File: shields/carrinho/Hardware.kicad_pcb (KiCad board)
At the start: 2 copper layers, 135.8 x 56.1 mm, 87 parts, among them J1 Conn_01x02, J10 Conn_01x04, J11 Conn_01x04, J12 Conn_02x13_Odd_Even, J13 Conn_01x02, J14 Conn_01x02, J2 Conn_01x04, J3 Conn_01x02, J4 Conn_01x02_Male, J5 Conn_01x02_Male, J6 Conn_01x02_Male, J7 Conn_01x02_Male, J8 Conn_01x03, J9 Conn_01x03, Q1 BD140, Q10 BC548, Q11 BD139, Q12 BD139, Q2 BD140, Q3 BC548, Q4 BC548, Q5 BD139, Q6 BD139, Q7 BD140, Q8 BD140, Q9 BC548, U1 LM393, U2 TCRT5000, U3 LM324, U4 HC-05, U5 TCRT5000

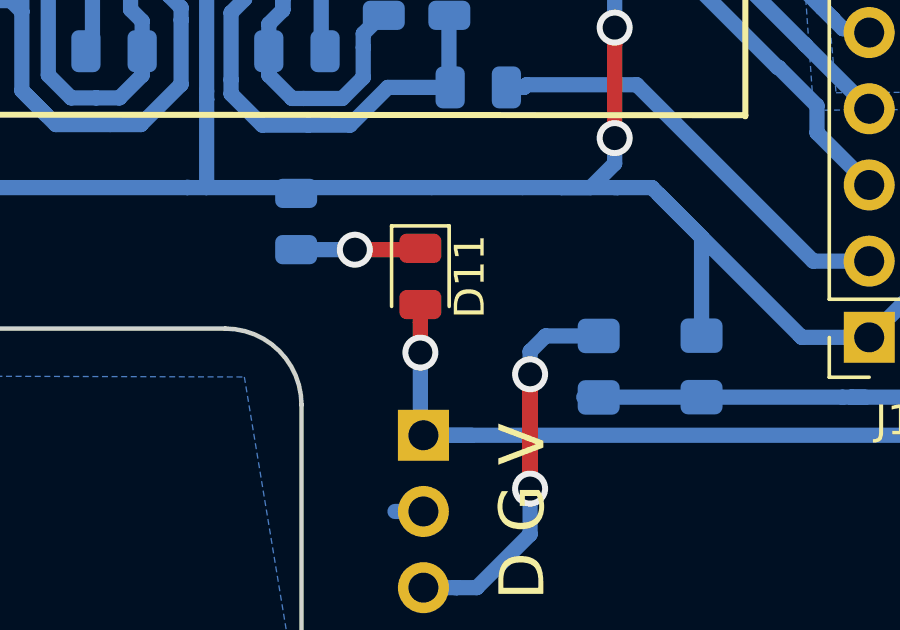
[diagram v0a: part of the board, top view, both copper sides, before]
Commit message: Adicionado exmplos com IRQ da USART.
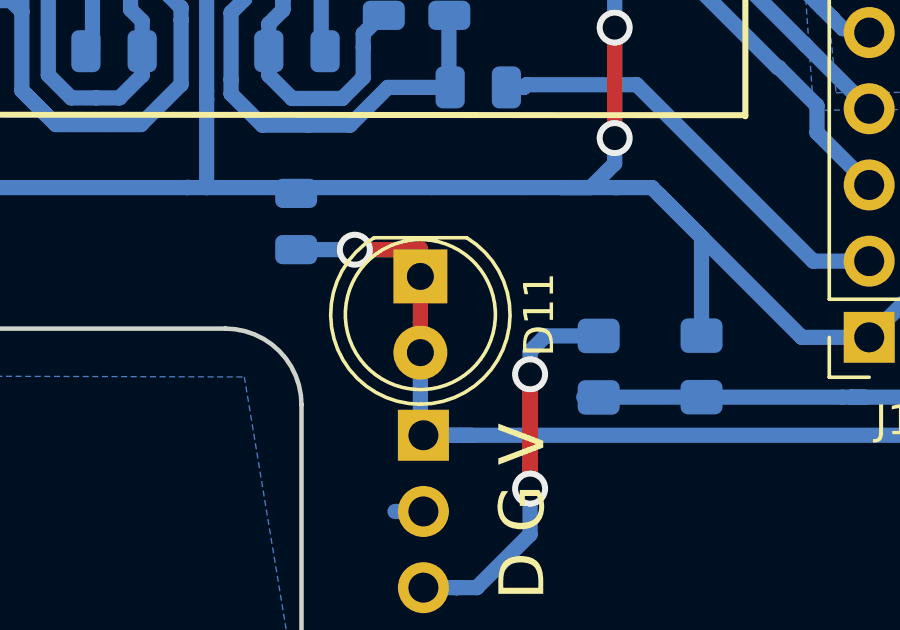
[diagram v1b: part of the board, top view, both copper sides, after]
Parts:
- D11: footprint LED_SMD:LED_0805_2012Metric -> LED_THT:LED_D5.0mm
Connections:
- D12 pad 1: +BATT -> Net-(D12-Pad1)
- D12 pad 2: Net-(D12-Pad2) -> +BATT
- J2 pad 1: Net-(D12-Pad2) -> +BATT
- J6 pad 1: +BATT -> Net-(D12-Pad1)
- J6 pad 2: +BATT -> Net-(D12-Pad1)
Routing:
- net Net-(D12-Pad2): track 4.70 -> 0.00 mm
- net +BATT: track 176.8 -> 181.5 mm
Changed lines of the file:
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@@
   (net 66 "Net-(D10-Pad2)")
   (net 67 "Net-(D11-Pad1)")
-  (net 68 "Net-(D12-Pad2)")
+  (net 68 "Net-(D12-Pad1)")
   (net_class Default "Esta é a classe de rede padrão."
     (clearance 0.3048)
@@
     (add_net "Net-(D10-Pad2)")
     (add_net "Net-(D11-Pad1)")
-    (add_net "Net-(D12-Pad2)")
+    (add_net "Net-(D12-Pad1)")
     (add_net "Net-(D2-Pad1)")
     (add_net "Net-(D5-Pad1)")
@@
   )
   (module LED_SMD:LED_0805_2012Metric (layer F.Cu)
-    (at 221.3102 73.2051 270)
-    (descr "LED SMD 0805 (2012 Metric), square (rectangular) end terminal, IPC_7351 nominal, (Body size source: https://docs.google.com/spreadsheets/d/1BsfQQcO9C6DZCsRaXUlFlo91Tg2WpOkGARC1WS5S8t0/edit?usp=sharing), generated with kicad-footprint-generator")
-    (tags diode)
-    (attr smd)
-    (fp_text reference D11 (at 0 -1.65 270) (layer F.SilkS)
-      (effects (font (size 1 1) (thickness 0.15)))
-    )
-    (fp_text value LED (at 0 1.65 270) (layer F.Fab)
-      (effects (font (size 1 1) (thickness 0.15)))
-    )
-    (fp_line (start 1 -0.6) (end -0.7 -0.6) (layer F.Fab) (width 0.1))
-    (fp_line (start -0.7 -0.6) (end -1 -0.3) (layer F.Fab) (width 0.1))
-    (fp_line (start -1 -0.3) (end -1 0.6) (layer F.Fab) (width 0.1))
-    (fp_line (start -1 0.6) (end 1 0.6) (layer F.Fab) (width 0.1))
-    (fp_line (start 1 0.6) (end 1 -0.6) (layer F.Fab) (width 0.1))
-    (fp_line (start 1 -0.96) (end -1.685 -0.96) (layer F.SilkS) (width 0.12))
-    (fp_line (start -1.685 -0.96) (end -1.685 0.96) (layer F.SilkS) (width 0.12))
-    (fp_line (start -1.685 0.96) (end 1 0.96) (layer F.SilkS) (width 0.12))
-    (fp_line (start -1.68 0.95) (end -1.68 -0.95) (layer F.CrtYd) (width 0.05))
-    (fp_line (start -1.68 -0.95) (end 1.68 -0.95) (layer F.CrtYd) (width 0.05))
-    (fp_line (start 1.68 -0.95) (end 1.68 0.95) (layer F.CrtYd) (width 0.05))
-    (fp_line (start 1.68 0.95) (end -1.68 0.95) (layer F.CrtYd) (width 0.05))
-    (fp_text user %R (at 0 0 270) (layer F.Fab)
-      (effects (font (size 0.5 0.5) (thickness 0.08)))
-    )
-    (pad 1 smd roundrect (at -0.9375 0 270) (size 0.975 1.4) (layers F.Cu F.Paste F.Mask) (roundrect_rratio 0.25)
-      (net 67 "Net-(D11-Pad1)"))
-    (pad 2 smd roundrect (at 0.9375 0 270) (size 0.975 1.4) (layers F.Cu F.Paste F.Mask) (roundrect_rratio 0.25)
-      (net 2 +5V))
-    (model ${KISYS3DMOD}/LED_SMD.3dshapes/LED_0805_2012Metric.wrl
-      (at (xyz 0 0 0))
-      (scale (xyz 1 1 1))
-      (rotate (xyz 0 0 0))
-    )
-  )
-  (module LED_SMD:LED_0805_2012Metric (layer F.Cu)
     (at 260.731 58.166 90)
     (descr "LED SMD 0805 (2012 Metric), square (rectangular) end terminal, IPC_7351 nominal, (Body size source: https://docs.google.com/spreadsheets/d/1BsfQQcO9C6DZCsRaXUlFlo91Tg2WpOkGARC1WS5S8t0/edit?usp=sharing), generated with kicad-footprint-generator")
@@
     (fp_line (start -3.55 2.15) (end 2.15 2.15) (layer B.SilkS) (width 0.12))
     (pad 1 smd rect (at -2.15 0 90) (size 2.5 2.3) (layers B.Cu B.Paste B.Mask)
-      (net 16 +BATT))
+      (net 68 "Net-(D12-Pad1)"))
     (pad 2 smd rect (at 2.15 0 90) (size 2.5 2.3) (layers B.Cu B.Paste B.Mask)
-      (net 68 "Net-(D12-Pad2)"))
+      (net 16 +BATT))
     (model ${KISYS3DMOD}/Diode_SMD.3dshapes/D_SMB.wrl
       (at (xyz 0 0 0))
@@
     (fp_line (start -1.27 -1.27) (end 0.635 -1.27) (layer F.Fab) (width 0.1))
     (pad 2 thru_hole oval (at 0 2.54) (size 1.7 1.7) (drill 1) (layers *.Cu *.Mask)
-      (net 16 +BATT))
+      (net 68 "Net-(D12-Pad1)"))
     (pad 1 thru_hole rect (at 0 0) (size 1.7 1.7) (drill 1) (layers *.Cu *.Mask)
-      (net 16 +BATT))
+      (net 68 "Net-(D12-Pad1)"))
     (model ${KISYS3DMOD}/Connector_PinSocket_2.54mm.3dshapes/PinSocket_1x02_P2.54mm_Vertical.wrl
       (at (xyz 0 0 0))
@@
       (net 22 BATMed))
     (pad 1 thru_hole rect (at 0 0 180) (size 1.7 1.7) (drill 1) (layers *.Cu *.Mask)
-      (net 68 "Net-(D12-Pad2)"))
+      (net 16 +BATT))
     (model ${KISYS3DMOD}/Connector_PinHeader_2.54mm.3dshapes/PinHeader_1x04_P2.54mm_Vertical.wrl
       (at (xyz 0 0 0))
@@
     )
   )
+  (module LED_THT:LED_D5.0mm (layer F.Cu)
+    (at 221.3102 73.2051 270)
+    (descr "LED, diameter 5.0mm, 2 pins, http://cdn-reichelt.de/documents/datenblatt/A500/LL-504BC2E-009.pdf")
+    (tags "LED diameter 5.0mm 2 pins")
+    (fp_text reference D11 (at 1.27 -3.96 270) (layer F.SilkS)
+      (effects (font (size 1 1) (thickness 0.15)))
+    )
+    (fp_text value LED (at 1.27 3.96 270) (layer F.Fab)
+      (effects (font (size 1 1) (thickness 0.15)))
+    )
+    (fp_arc (start 1.27 0) (end -1.23 -1.469694) (angle 299.1) (layer F.Fab) (width 0.1))
+    (fp_arc (start 1.27 0) (end -1.29 -1.54483) (angle 148.9) (layer F.SilkS) (width 0.12))
+    (fp_arc (start 1.27 0) (end -1.29 1.54483) (angle -148.9) (layer F.SilkS) (width 0.12))
+    (fp_circle (center 1.27 0) (end 3.77 0) (layer F.Fab) (width 0.1))
+    (fp_circle (center 1.27 0) (end 3.77 0) (layer F.SilkS) (width 0.12))
+    (fp_line (start -1.23 -1.469694) (end -1.23 1.469694) (layer F.Fab) (width 0.1))
+    (fp_line (start -1.29 -1.545) (end -1.29 1.545) (layer F.SilkS) (width 0.12))
+    (fp_line (start -1.95 -3.25) (end -1.95 3.25) (layer F.CrtYd) (width 0.05))
+    (fp_line (start -1.95 3.25) (end 4.5 3.25) (layer F.CrtYd) (width 0.05))
+    (fp_line (start 4.5 3.25) (end 4.5 -3.25) (layer F.CrtYd) (width 0.05))
+    (fp_line (start 4.5 -3.25) (end -1.95 -3.25) (layer F.CrtYd) (width 0.05))
+    (fp_text user %R (at 1.25 0 270) (layer F.Fab)
+      (effects (font (size 0.8 0.8) (thickness 0.2)))
+    )
+    (pad 1 thru_hole rect (at 0 0 270) (size 1.8 1.8) (drill 0.9) (layers *.Cu *.Mask)
+      (net 67 "Net-(D11-Pad1)"))
+    (pad 2 thru_hole circle (at 2.54 0 270) (size 1.8 1.8) (drill 0.9) (layers *.Cu *.Mask)
+      (net 2 +5V))
+    (model ${KISYS3DMOD}/LED_THT.3dshapes/LED_D5.0mm.wrl
+      (at (xyz 0 0 0))
+      (scale (xyz 1 1 1))
+      (rotate (xyz 0 0 0))
+    )
+  )
   (gr_line (start 266.0142 34.3154) (end 266.0142 85.3694) (layer Edge.Cuts) (width 0.15))
   (gr_arc (start 220.0148 34.3027) (end 220.0148 31.7627) (angle -90) (layer Edge.Cuts) (width 0.15))
@@
   (segment (start 221.264 72.3138) (end 221.3102 72.2676) (width 0.508) (layer F.Cu) (net 67))
   (segment (start 219.1258 72.3138) (end 221.264 72.3138) (width 0.508) (layer F.Cu) (net 67))
-  (segment (start 167.64 63.7667) (end 167.64 68.462) (width 0.508) (layer B.Cu) (net 68))
+  (segment (start 167.64 63.7667) (end 167.64 68.462) (width 0.508) (layer B.Cu) (net 16))
   (zone (net 16) (net_name +BATT) (layer B.Cu) (hatch edge 0.508)
     (connect_pads (clearance 0.3048))
